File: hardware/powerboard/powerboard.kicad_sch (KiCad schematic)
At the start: 43 parts, among them J1 USB_B_Micro, J2 Boot Header, J3 Power Header, J4 SPI Header, SW1 Oct_Up, SW2 RESET, SW3 Oct_Down, U2 MCP1603, U3 RP2040, U4 W25Q128JVSIM, Y1 ABLS-12.000MHZ-B4-T

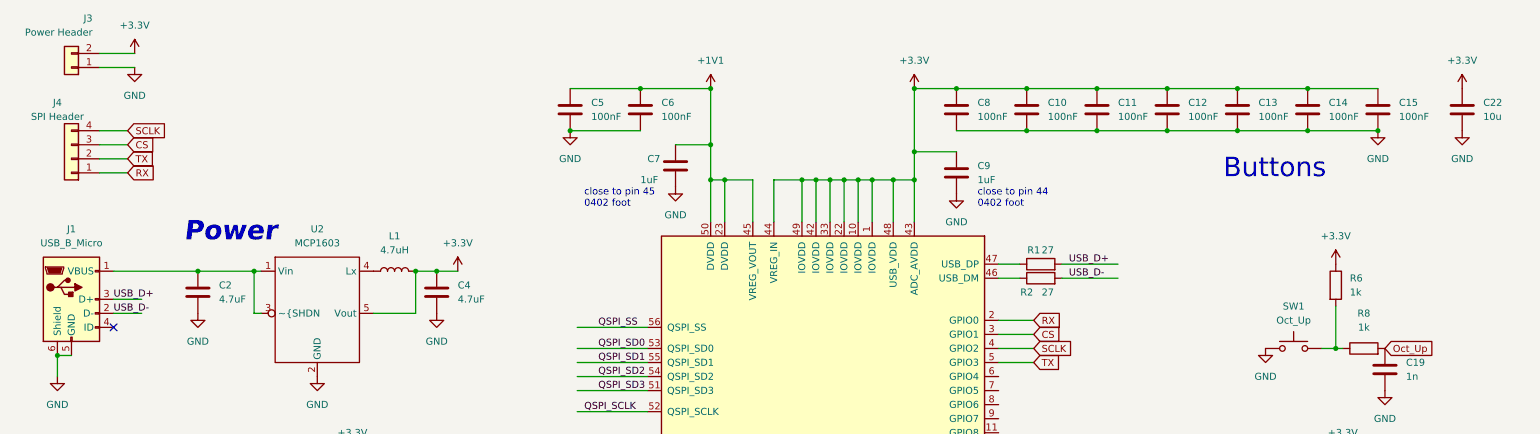
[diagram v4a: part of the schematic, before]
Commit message: More PCB Layout
Board Overhauled
Crystal Routed
Bypass Caps on Bottom of Board
Everything but switches done
ANNULAR RING PROBLEM
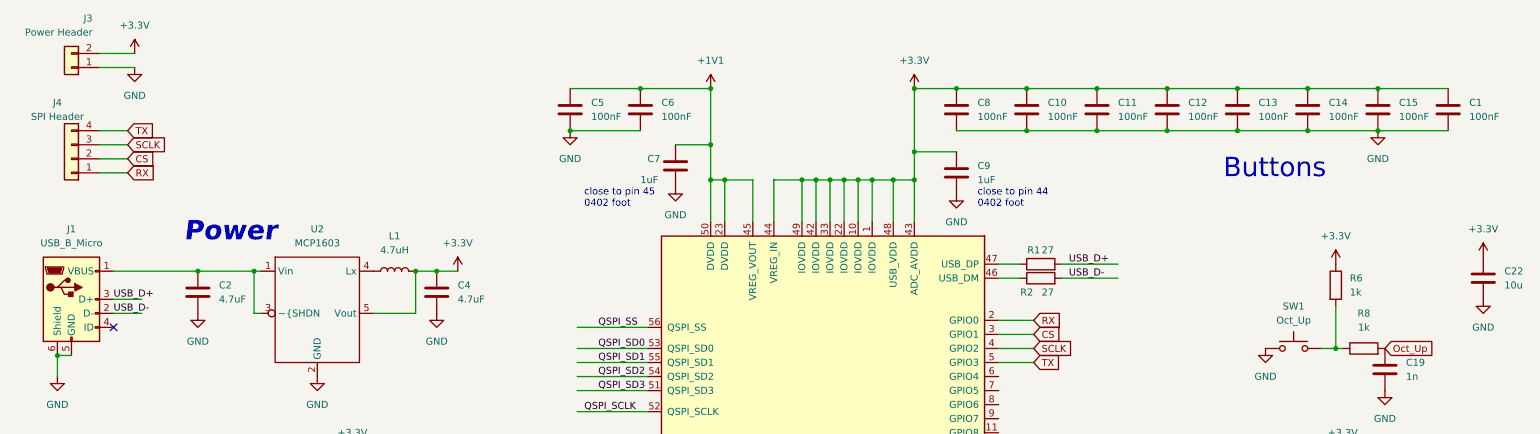
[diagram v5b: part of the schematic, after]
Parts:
- added C1: 100nF, Capacitor_SMD:C_0402_1005Metric, symbol Device:C
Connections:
- net +3.3V: now also C1.1
- net CS: now also J4.2 (Pin_2); no longer J4.3 (Pin_3)
- net GND: now also C1.2
- net SCLK: now also J4.3 (Pin_3); no longer J4.4 (Pin_4)
- net TX: now also J4.4 (Pin_4); no longer J4.2 (Pin_2)
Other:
- moved on the sheet: C22
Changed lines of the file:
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@@
   (junction (at 72.39 161.29) (diameter 0) (color 0 0 0 0)
+  )
+  (junction (at 259.08 29.21) (diameter 0) (color 0 0 0 0)
   )
   (junction (at 57.15 168.91) (diameter 0) (color 0 0 0 0)
@@
     (stroke (width 0) (type default) (color 0 0 0 0))
   )
+  (wire (pts (xy 259.08 29.21) (xy 271.78 29.21))
+    (stroke (width 0) (type default) (color 0 0 0 0))
+  )
   (wire (pts (xy 157.48 45.72) (xy 157.48 53.34))
     (stroke (width 0) (type default) (color 0 0 0 0))
@@
     (stroke (width 0) (type default) (color 0 0 0 0))
   )
-  (wire (pts (xy 33.02 36.83) (xy 27.94 36.83))
-    (stroke (width 0) (type default) (color 0 0 0 0))
-  )
   (wire (pts (xy 55.88 69.85) (xy 57.15 69.85))
     (stroke (width 0) (type default) (color 0 0 0 0))
@@
     (stroke (width 0) (type default) (color 0 0 0 0))
   )
+  (wire (pts (xy 27.94 39.37) (xy 33.02 39.37))
+    (stroke (width 0) (type default) (color 0 0 0 0))
+  )
   (wire (pts (xy 198.12 127) (xy 190.5 127))
     (stroke (width 0) (type default) (color 0 0 0 0))
@@
     (stroke (width 0) (type default) (color 0 0 0 0))
   )
-  (wire (pts (xy 33.02 39.37) (xy 27.94 39.37))
-    (stroke (width 0) (type default) (color 0 0 0 0))
-  )
   (wire (pts (xy 167.64 45.72) (xy 167.64 53.34))
     (stroke (width 0) (type default) (color 0 0 0 0))
@@
     (stroke (width 0) (type default) (color 0 0 0 0))
   )
-  (wire (pts (xy 33.02 41.91) (xy 27.94 41.91))
-    (stroke (width 0) (type default) (color 0 0 0 0))
-  )
   (wire (pts (xy 73.66 100.33) (xy 73.66 102.87))
     (stroke (width 0) (type default) (color 0 0 0 0))
@@
     (stroke (width 0) (type default) (color 0 0 0 0))
   )
+  (wire (pts (xy 27.94 36.83) (xy 33.02 36.83))
+    (stroke (width 0) (type default) (color 0 0 0 0))
+  )
   (wire (pts (xy 92.71 115.57) (xy 105.41 115.57))
     (stroke (width 0) (type default) (color 0 0 0 0))
   )
+  (wire (pts (xy 27.94 41.91) (xy 33.02 41.91))
+    (stroke (width 0) (type default) (color 0 0 0 0))
+  )
   (wire (pts (xy 138.43 45.72) (xy 138.43 39.37))
     (stroke (width 0) (type default) (color 0 0 0 0))
@@
   )
   (wire (pts (xy 252.73 76.2) (xy 251.46 76.2))
+    (stroke (width 0) (type default) (color 0 0 0 0))
+  )
+  (wire (pts (xy 259.08 36.83) (xy 271.78 36.83))
     (stroke (width 0) (type default) (color 0 0 0 0))
   )
@@
     )
   )
-  (global_label "TX" (shape input) (at 33.02 41.91 0) (fields_autoplaced)
+  (global_label "TX" (shape input) (at 33.02 36.83 0) (fields_autoplaced)
     (effects (font (size 1.27 1.27)) (justify left))
-    (property "Intersheet References" "${INTERSHEET_REFS}" (id 0) (at 37.6102 41.8306 0)
+    (property "Intersheet References" "${INTERSHEET_REFS}" (id 0) (at 37.6102 36.7506 0)
       (effects (font (size 1.27 1.27)) (justify left) hide)
     )
   )
-  (global_label "SCLK" (shape input) (at 33.02 36.83 0) (fields_autoplaced)
+  (global_label "SCLK" (shape input) (at 33.02 39.37 0) (fields_autoplaced)
     (effects (font (size 1.27 1.27)) (justify left))
-    (property "Intersheet References" "${INTERSHEET_REFS}" (id 0) (at 40.2107 36.7506 0)
+    (property "Intersheet References" "${INTERSHEET_REFS}" (id 0) (at 40.2107 39.2906 0)
       (effects (font (size 1.27 1.27)) (justify left) hide)
     )
@@
     )
   )
-  (global_label "CS" (shape input) (at 33.02 39.37 0) (fields_autoplaced)
+  (global_label "CS" (shape input) (at 33.02 41.91 0) (fields_autoplaced)
     (effects (font (size 1.27 1.27)) (justify left))
-    (property "Intersheet References" "${INTERSHEET_REFS}" (id 0) (at 37.9126 39.2906 0)
+    (property "Intersheet References" "${INTERSHEET_REFS}" (id 0) (at 37.9126 41.8306 0)
       (effects (font (size 1.27 1.27)) (justify left) hide)
     )
@@
     (pin "1")
   )
-  (symbol (lib_id "power:+3.3V") (at 274.32 29.21 0) (unit 1)
-    (in_bom yes) (on_board yes) (fields_autoplaced)
-    (property "Reference" "#PWR033" (id 0) (at 274.32 33.02 0)
-      (effects (font (size 1.27 1.27)) hide)
-    )
-    (property "Value" "+3.3V" (id 1) (at 274.32 24.13 0))
-    (property "Footprint" "" (id 2) (at 274.32 29.21 0)
-      (effects (font (size 1.27 1.27)) hide)
-    )
-    (property "Datasheet" "" (id 3) (at 274.32 29.21 0)
+  (symbol (lib_id "power:+3.3V") (at 278.13 59.69 0) (unit 1)
+    (in_bom yes) (on_board yes) (fields_autoplaced)
+    (property "Reference" "#PWR033" (id 0) (at 278.13 63.5 0)
+      (effects (font (size 1.27 1.27)) hide)
+    )
+    (property "Value" "+3.3V" (id 1) (at 278.13 54.61 0))
+    (property "Footprint" "" (id 2) (at 278.13 59.69 0)
+      (effects (font (size 1.27 1.27)) hide)
+    )
+    (property "Datasheet" "" (id 3) (at 278.13 59.69 0)
       (effects (font (size 1.27 1.27)) hide)
     )
@@
     (pin "2")
   )
+  (symbol (lib_id "Device:C") (at 271.78 33.02 0) (unit 1)
+    (in_bom yes) (on_board yes) (fields_autoplaced)
+    (property "Reference" "C1" (id 0) (at 275.59 31.7499 0)
+      (effects (font (size 1.27 1.27)) (justify left))
+    )
+    (property "Value" "100nF" (id 1) (at 275.59 34.2899 0)
+      (effects (font (size 1.27 1.27)) (justify left))
+    )
+    (property "Footprint" "Capacitor_SMD:C_0402_1005Metric" (id 2) (at 272.7452 36.83 0)
+      (effects (font (size 1.27 1.27)) hide)
+    )
+    (property "Datasheet" "~" (id 3) (at 271.78 33.02 0)
+      (effects (font (size 1.27 1.27)) hide)
+    )
+    (pin "1")
+    (pin "2")
+  )
   (symbol (lib_id "Switch:SW_Push") (at 245.11 110.49 0) (unit 1)
     (in_bom yes) (on_board yes) (fields_autoplaced)
@@
     (pin "2")
   )
-  (symbol (lib_id "Device:C") (at 274.32 33.02 0) (unit 1)
-    (in_bom yes) (on_board yes) (fields_autoplaced)
-    (property "Reference" "C22" (id 0) (at 278.13 31.7499 0)
-      (effects (font (size 1.27 1.27)) (justify left))
-    )
-    (property "Value" "10u" (id 1) (at 278.13 34.2899 0)
-      (effects (font (size 1.27 1.27)) (justify left))
-    )
-    (property "Footprint" "Capacitor_SMD:C_0603_1608Metric" (id 2) (at 275.2852 36.83 0)
-      (effects (font (size 1.27 1.27)) hide)
-    )
-    (property "Datasheet" "~" (id 3) (at 274.32 33.02 0)
+  (symbol (lib_id "Device:C") (at 278.13 63.5 0) (unit 1)
+    (in_bom yes) (on_board yes) (fields_autoplaced)
+    (property "Reference" "C22" (id 0) (at 281.94 62.2299 0)
+      (effects (font (size 1.27 1.27)) (justify left))
+    )
+    (property "Value" "10u" (id 1) (at 281.94 64.7699 0)
+      (effects (font (size 1.27 1.27)) (justify left))
+    )
+    (property "Footprint" "Capacitor_SMD:C_0603_1608Metric" (id 2) (at 279.0952 67.31 0)
+      (effects (font (size 1.27 1.27)) hide)
+    )
+    (property "Datasheet" "~" (id 3) (at 278.13 63.5 0)
       (effects (font (size 1.27 1.27)) hide)
     )
@@
     (pin "4")
   )
-  (symbol (lib_id "power:GND") (at 274.32 36.83 0) (unit 1)
-    (in_bom yes) (on_board yes) (fields_autoplaced)
-    (property "Reference" "#PWR034" (id 0) (at 274.32 43.18 0)
-      (effects (font (size 1.27 1.27)) hide)
-    )
-    (property "Value" "GND" (id 1) (at 274.32 41.91 0))
-    (property "Footprint" "" (id 2) (at 274.32 36.83 0)
-      (effects (font (size 1.27 1.27)) hide)
-    )
-    (property "Datasheet" "" (id 3) (at 274.32 36.83 0)
+  (symbol (lib_id "power:GND") (at 278.13 67.31 0) (unit 1)
+    (in_bom yes) (on_board yes) (fields_autoplaced)
+    (property "Reference" "#PWR034" (id 0) (at 278.13 73.66 0)
+      (effects (font (size 1.27 1.27)) hide)
+    )
+    (property "Value" "GND" (id 1) (at 278.13 72.39 0))
+    (property "Footprint" "" (id 2) (at 278.13 67.31 0)
+      (effects (font (size 1.27 1.27)) hide)
+    )
+    (property "Datasheet" "" (id 3) (at 278.13 67.31 0)
       (effects (font (size 1.27 1.27)) hide)
     )
@@
       (reference "#PWR0103") (unit 1) (value "+3.3V") (footprint "")
     )
+    (path "/83cabe1d-1125-4aec-a015-e49881d7458f"
+      (reference "C1") (unit 1) (value "100nF") (footprint "Capacitor_SMD:C_0402_1005Metric")
+    )
     (path "/3057d2bb-7d2c-4c6c-8f62-077e90d33791"

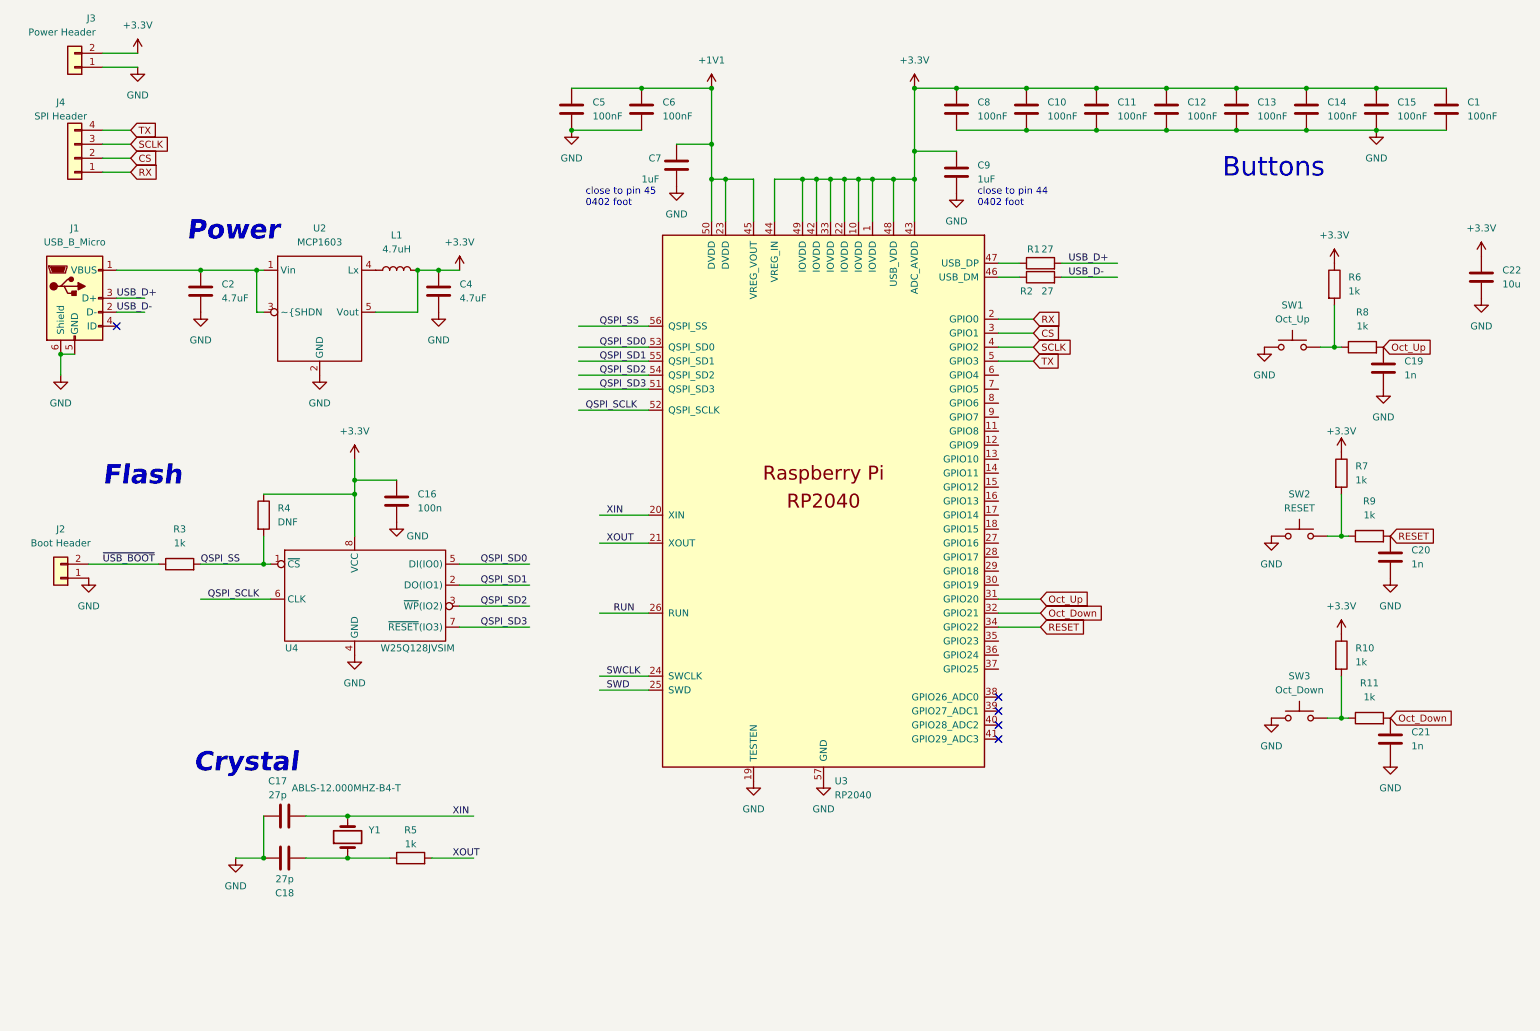
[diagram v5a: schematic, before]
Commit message: Power PCB: Everything(?!) Placed
Added SPI_0 and SPI_1 Headers, for ADC and Display
Added I2C_0 and I2C_1 Headers, for possible future peripherals, and/or 4 GPIO Pins.
I assume we don't need UART for anything, so I left it un-routed.
Everything placed I hope(?), just need to route the buttons and adjust copper zones.
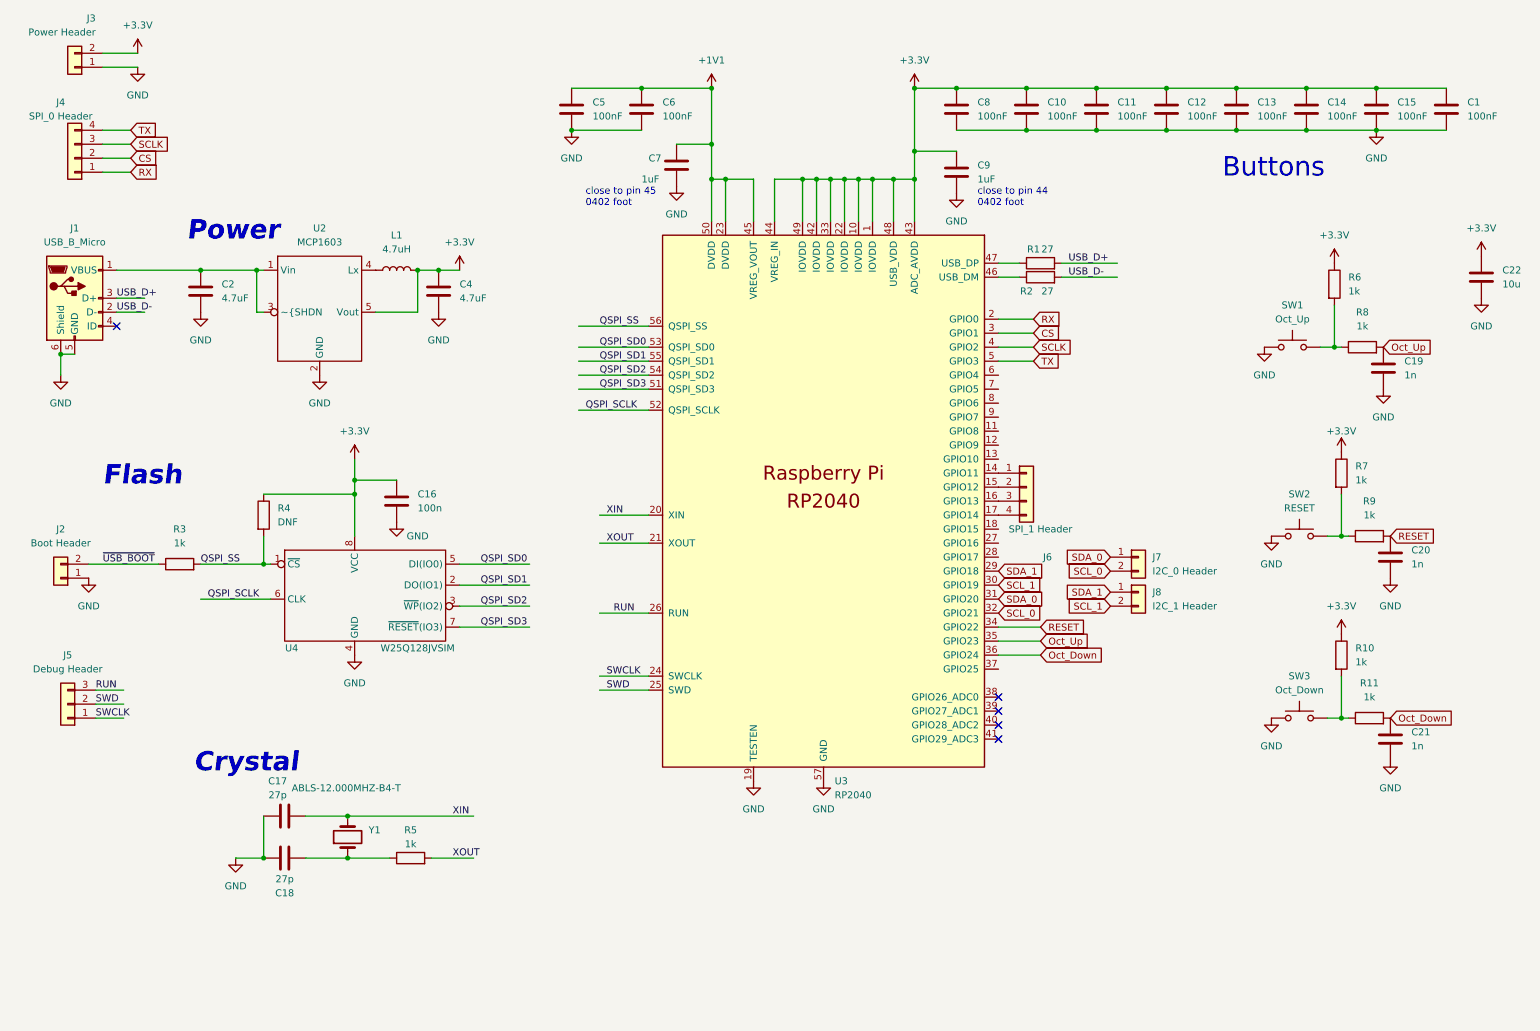
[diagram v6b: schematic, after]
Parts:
- added J5: Debug Header, Connector_PinHeader_2.54mm:PinHeader_1x03_P2.54mm_Vertical, symbol Connector_Generic:Conn_01x03
- added J6: SPI_1 Header, Connector_PinHeader_2.54mm:PinHeader_1x04_P2.54mm_Vertical, symbol Connector_Generic:Conn_01x04
- added J7: I2C_0 Header, Connector_PinHeader_2.54mm:PinHeader_1x02_P2.54mm_Vertical, symbol Connector_Generic:Conn_01x02
- added J8: I2C_1 Header, Connector_PinHeader_2.54mm:PinHeader_1x02_P2.54mm_Vertical, symbol Connector_Generic:Conn_01x02
- J4: value SPI Header -> SPI_0 Header
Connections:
- net Oct_Down: now also U3.36 (GPIO24); no longer U3.32 (GPIO21)
- net Oct_Up: now also U3.35 (GPIO23); no longer U3.31 (GPIO20)
- net RUN: now also J5.3 (Pin_3)
- net SWCLK: now also J5.1 (Pin_1)
- net SWD: now also J5.2 (Pin_2)
- net at U3.14 (GPIO11): now also J6.1 (Pin_1)
- net at U3.15 (GPIO12): now also J6.2 (Pin_2)
- net at U3.16 (GPIO13): now also J6.3 (Pin_3)
- net at U3.17 (GPIO14): now also J6.4 (Pin_4)
- net SDA_1: now reaches U3.29 (GPIO18)
- net SDA_1: now also J8.1 (Pin_1)
- net SCL_1: now reaches U3.30 (GPIO19)
- net SCL_1: now also J8.2 (Pin_2)
- new net SCL_0: J7.2 (Pin_2), U3.32 (GPIO21)
- new net SDA_0: J7.1 (Pin_1), U3.31 (GPIO20)

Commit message: PCB Adjustments
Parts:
- added C23, C24, C3: 100n, Capacitor_SMD:C_0603_1608Metric, symbol Device:C
- added R12: 10k, Resistor_SMD:R_0402_1005Metric, symbol Device:R
- added R13, R14: 10k, Resistor_SMD:R_0603_1608Metric, symbol Device:R
- added SW4: RotaryEncoder_Switch, Rotary_Encoder:RotaryEncoder_Alps_EC11E-Switch_Vertical_H20mm, symbol Device:RotaryEncoder_Switch
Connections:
- net +3.3V: now also R12.1, R13.1, R14.1
- net GND: now also C23.2, C24.2, C3.2, SW4.C, SW4.S2
- net Encoder_Press: now reaches U3.38 (GPIO26_ADC0)
- net Encoder_Press: now also C3.1, R12.2, SW4.S1
- net B: now reaches U3.39 (GPIO27_ADC1)
- net B: now also C24.1, R14.2, SW4.B
- net A: now reaches U3.40 (GPIO28_ADC2)
- net A: now also C23.1, R13.2, SW4.A
- no-connect marks 5 -> 2
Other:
- moved on the sheet: C17, C18, R5, Y1

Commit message: USB Header Footprint Changed
Found a USB Header on JLCAssembly that has a matching footprint in KiCad, W
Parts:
- J1: footprint Connector_USB:USB_Micro-B_Molex_47346-0001 -> Connector_USB:USB_Micro-B_Amphenol_10118194_Horizontal
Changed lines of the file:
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@@
     (property "Reference" "J1" (id 0) (at 22.86 54.61 0))
     (property "Value" "USB_B_Micro" (id 1) (at 22.86 57.15 0))
-    (property "Footprint" "Connector_USB:USB_Micro-B_Molex_47346-0001" (id 2) (at 26.67 68.58 0)
+    (property "Footprint" "Connector_USB:USB_Micro-B_Amphenol_10118194_Horizontal" (id 2) (at 26.67 68.58 0)
       (effects (font (size 1.27 1.27)) hide)
     )
@@
     )
     (path "/76040476-116c-4e4a-b862-69aacc221299"
-      (reference "J1") (unit 1) (value "USB_B_Micro") (footprint "Connector_USB:USB_Micro-B_Molex_47346-0001")
+      (reference "J1") (unit 1) (value "USB_B_Micro") (footprint "Connector_USB:USB_Micro-B_Amphenol_10118194_Horizontal")
     )
     (path "/abc16ad4-cd43-463c-940b-c8c7941313d7"
